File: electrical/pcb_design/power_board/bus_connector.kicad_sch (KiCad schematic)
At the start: 20 parts, among them J1 TE_Connectivity_7-5530843-7, J2 TE_Connectivity_7-5530843-7, J3 TE_Connectivity_7-5530843-7, J4 TE_Connectivity_7-5530843-7, J5 TE_Connectivity_7-5530843-7, J6 TE_Connectivity_7-5530843-7, J7 TE_Connectivity_7-5530843-7, J8 TE_Connectivity_7-5530843-7, U1 TCAN330

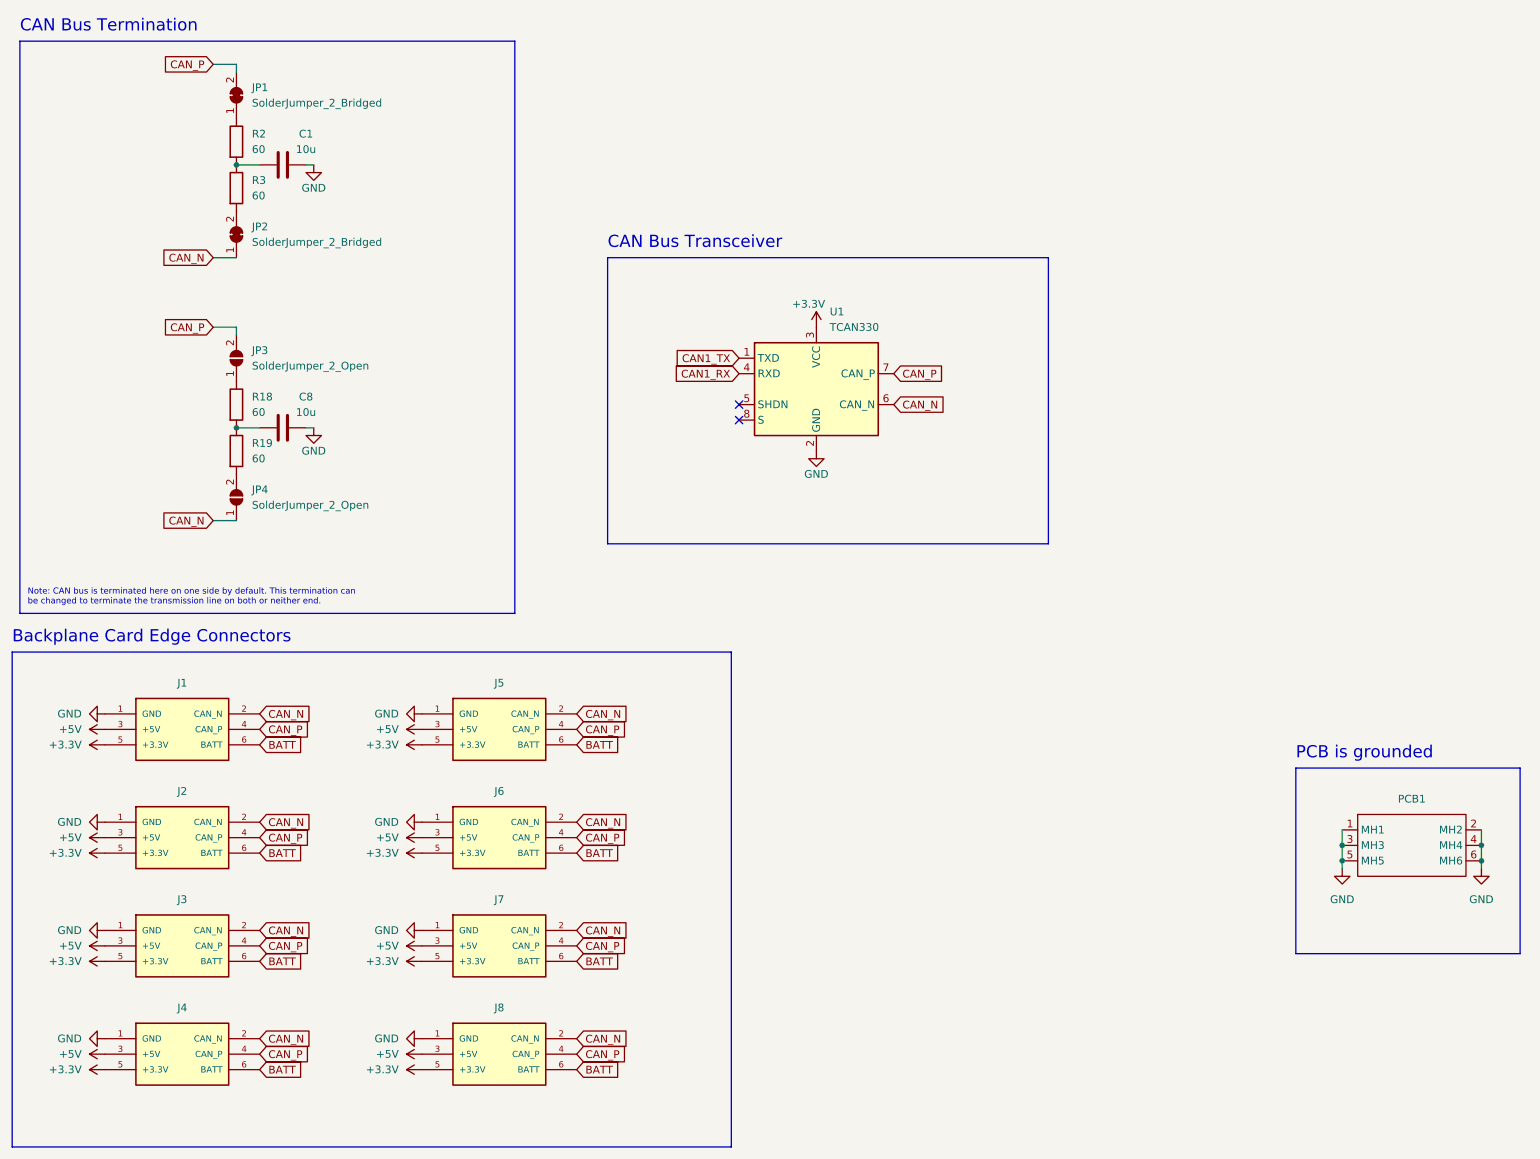
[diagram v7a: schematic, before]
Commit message: Updated symbols and footprints of many parts
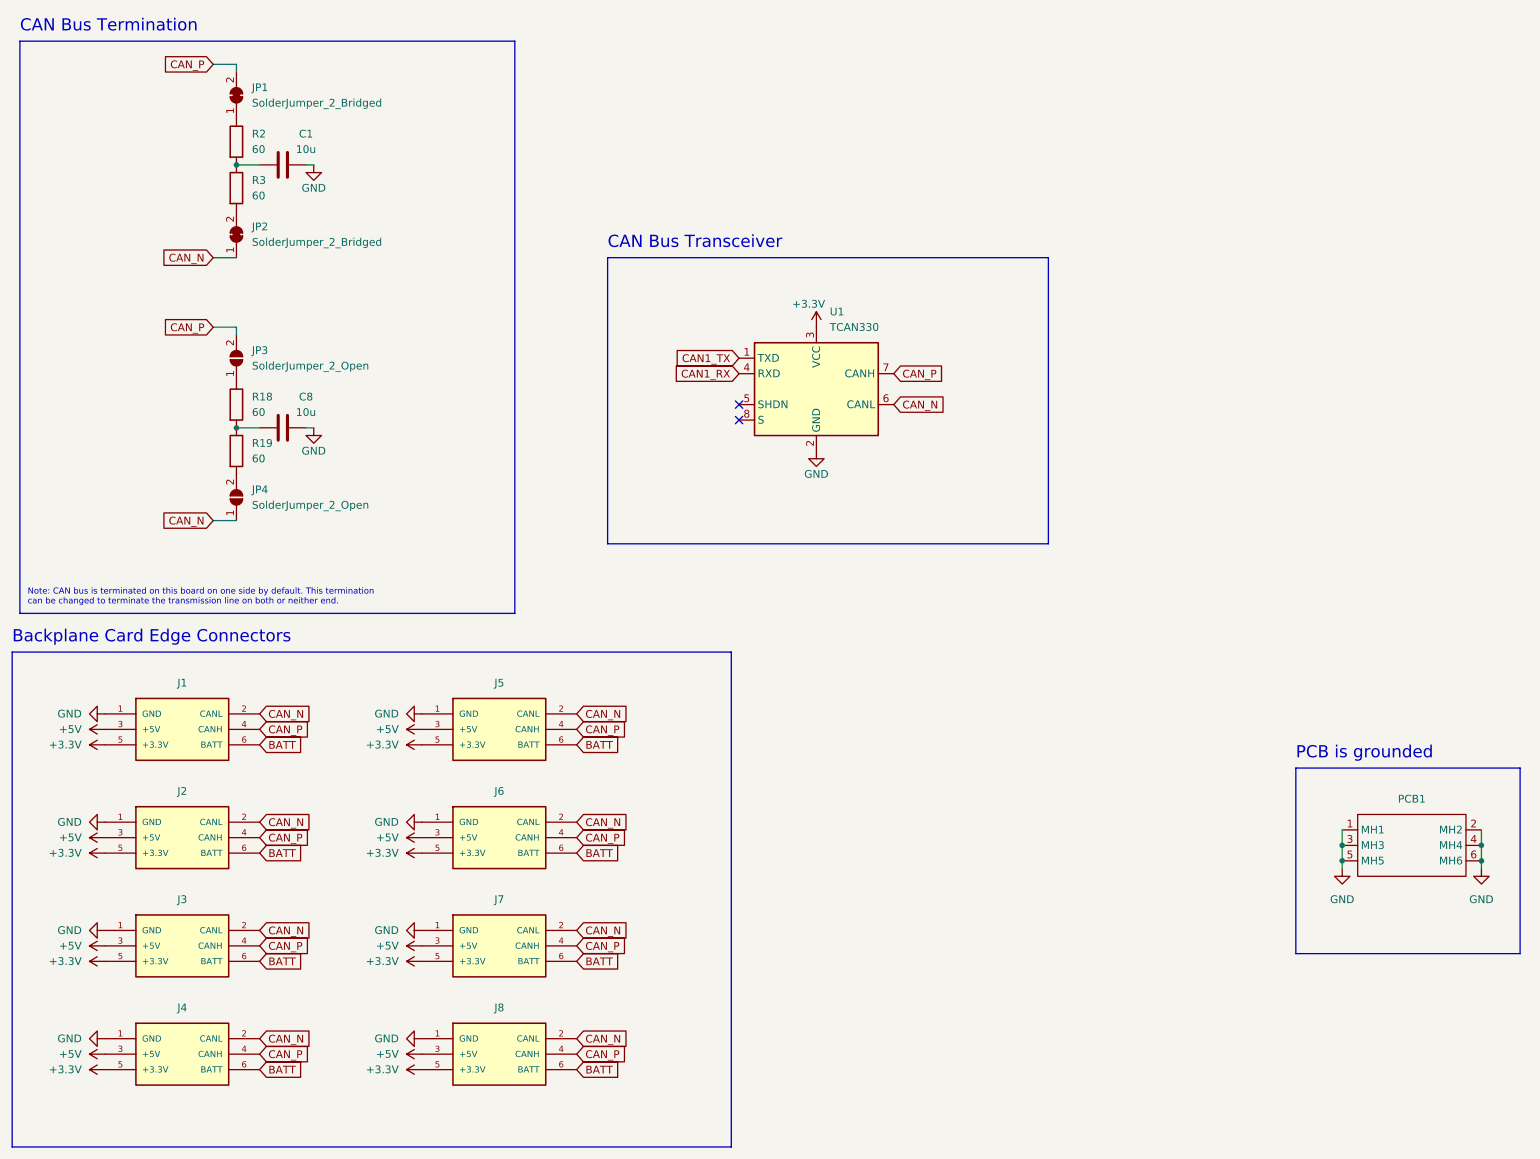
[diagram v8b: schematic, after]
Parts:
- C1, C8: footprint Capacitor_SMD:C_0603_1608Metric -> footprints:Nondescript_C_0603_1608Metric; symbol Device:C -> TVSC:Large_Decoupling_Capacitor; MPN C19702 -> C344022; Manufacturer Samsung Electro-Mechanics -> Murata Electronics; Manufacturer Part Number CL10A106KP8NNNC -> GRM188R61E106KA73D
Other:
- note added: "Note: CAN bus is terminated on this board on one side by default. This termination can be changed to terminate the transmission line on both or neither end."
- note removed: "Note: CAN bus is terminated here on one side by default. This termination can be changed to terminate the transmission line on both or neither end."
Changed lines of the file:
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@@
     (fill (type none))
   )
-  (text "Note: CAN bus is terminated here on one side by default. This termination can\nbe changed to terminate the transmission line on both or neither end."
+  (text "Note: CAN bus is terminated on this board on one side by default. This termination\ncan be changed to terminate the transmission line on both or neither end."
     (at 17.78 111.76 0)
     (effects (font (size 1 1)) (justify left bottom))
@@
     )
   )
-  (symbol (lib_id "Device:C") (at 59.69 39.37 90) (unit 1)
+  (symbol (lib_id "TVSC:Large_Decoupling_Capacitor") (at 59.69 39.37 90) (unit 1)
     (in_bom yes) (on_board yes) (dnp no)
     (property "Reference" "C1" (at 63.5 34.29 90)
@@
       (effects (font (size 1.27 1.27)))
     )
-    (property "Footprint" "Capacitor_SMD:C_0603_1608Metric" (at 63.5 38.4048 0)
-      (effects (font (size 1.27 1.27)) hide)
-    )
-    (property "Datasheet" "~" (at 59.69 39.37 0)
-      (effects (font (size 1.27 1.27)) hide)
-    )
-    (property "MPN" "C19702" (at 59.69 39.37 0)
-      (effects (font (size 1.27 1.27)) hide)
-    )
-    (property "Manufacturer" "Samsung Electro-Mechanics" (at 59.69 39.37 0)
-      (effects (font (size 1.27 1.27)) hide)
-    )
-    (property "Manufacturer Part Number" "CL10A106KP8NNNC" (at 59.69 39.37 0)
+    (property "Footprint" "footprints:Nondescript_C_0603_1608Metric" (at 66.04 39.37 0)
+      (effects (font (size 1.27 1.27)) hide)
+    )
+    (property "Datasheet" "https://www.murata.com/en-us/products/productdetail?partno=GRM188R61E106KA73%23" (at 76.2 39.37 0)
+      (effects (font (size 1.27 1.27)) hide)
+    )
+    (property "MPN" "C344022" (at 73.66 39.37 0)
+      (effects (font (size 1.27 1.27)) hide)
+    )
+    (property "Manufacturer" "Murata Electronics" (at 68.58 39.37 0)
+      (effects (font (size 1.27 1.27)) hide)
+    )
+    (property "Manufacturer Part Number" "GRM188R61E106KA73D" (at 71.12 39.37 0)
       (effects (font (size 1.27 1.27)) hide)
     )
@@
     )
   )
-  (symbol (lib_id "Device:C") (at 59.69 82.55 90) (unit 1)
+  (symbol (lib_id "TVSC:Large_Decoupling_Capacitor") (at 59.69 82.55 90) (unit 1)
     (in_bom yes) (on_board yes) (dnp no)
     (property "Reference" "C8" (at 63.5 77.47 90)
@@
       (effects (font (size 1.27 1.27)))
     )
-    (property "Footprint" "Capacitor_SMD:C_0603_1608Metric" (at 63.5 81.5848 0)
-      (effects (font (size 1.27 1.27)) hide)
-    )
-    (property "Datasheet" "~" (at 59.69 82.55 0)
-      (effects (font (size 1.27 1.27)) hide)
-    )
-    (property "MPN" "C19702" (at 59.69 82.55 0)
-      (effects (font (size 1.27 1.27)) hide)
-    )
-    (property "Manufacturer" "Samsung Electro-Mechanics" (at 59.69 82.55 0)
-      (effects (font (size 1.27 1.27)) hide)
-    )
-    (property "Manufacturer Part Number" "CL10A106KP8NNNC" (at 59.69 82.55 0)
+    (property "Footprint" "footprints:Nondescript_C_0603_1608Metric" (at 66.04 82.55 0)
+      (effects (font (size 1.27 1.27)) hide)
+    )
+    (property "Datasheet" "https://www.murata.com/en-us/products/productdetail?partno=GRM188R61E106KA73%23" (at 76.2 82.55 0)
+      (effects (font (size 1.27 1.27)) hide)
+    )
+    (property "MPN" "C344022" (at 73.66 82.55 0)
+      (effects (font (size 1.27 1.27)) hide)
+    )
+    (property "Manufacturer" "Murata Electronics" (at 68.58 82.55 0)
+      (effects (font (size 1.27 1.27)) hide)
+    )
+    (property "Manufacturer Part Number" "GRM188R61E106KA73D" (at 71.12 82.55 0)
       (effects (font (size 1.27 1.27)) hide)
     )
@@
       (effects (font (size 1.27 1.27) italic) hide)
     )
-    (property "Datasheet" "https://www.ti.com/lit/ds/symlink/tcan330.pdf" (at 147.32 76.2 0)
-      (effects (font (size 1.27 1.27)) hide)
-    )
+    (property "Datasheet" "http://www.ti.com/lit/ds/symlink/tcan330.pdf" (at 147.32 76.2 0)
+      (effects (font (size 1.27 1.27)) hide)
+    )
